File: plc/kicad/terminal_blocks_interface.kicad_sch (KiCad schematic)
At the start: 75 parts, among them CN1 DB128V-5.08-6P-GN-S, CN10 DB128V-5.08-2P-GN-S, CN4 KF128-5.0-3P, CN5 KF128-5.0-3P, CN7 DB128V-5.08-2P-GN-S, CN8 DB128V-5.08-2P-GN-S, CN9 DB128V-5.08-2P-GN-S, Q1 AO3400A, Q2 AO3400A, U1 LTV-814S-TA1-A, U10 LTV-814S-TA1-A, U4 ADS1115IDGSR, U5 TPS272C45DRHFR, U6 TPS272C45DRHFR, U7 TCA9535PWR, U8 LTV-814S-TA1-A, U9 LTV-814S-TA1-A

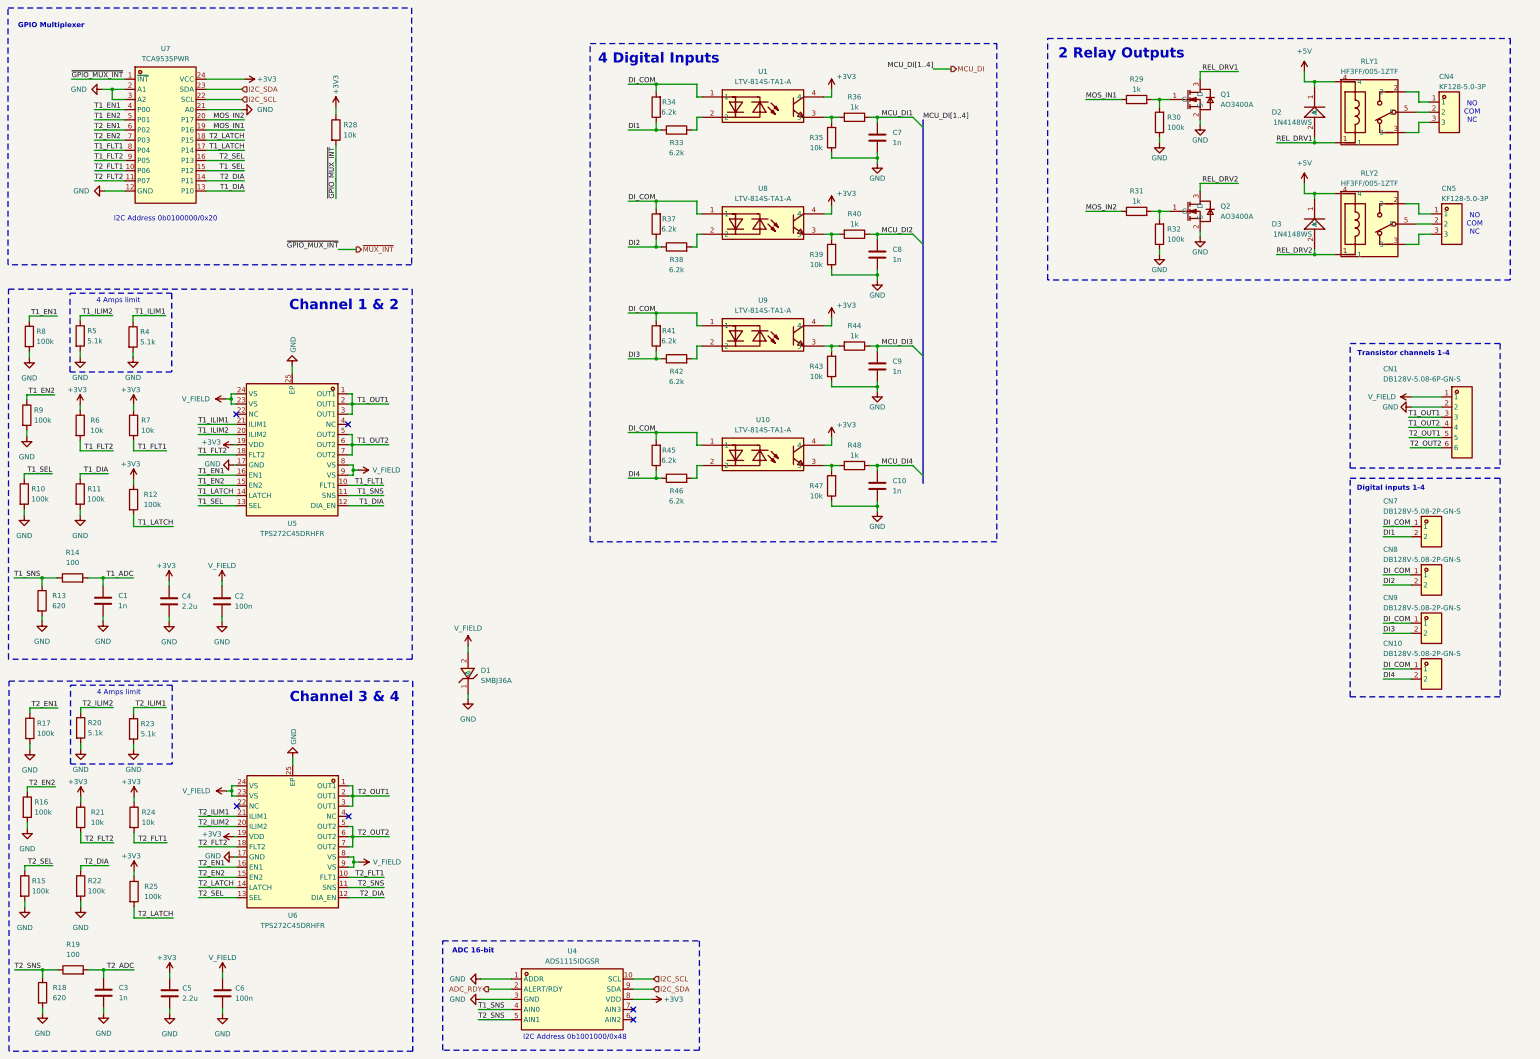
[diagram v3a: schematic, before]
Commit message: Added netclasses
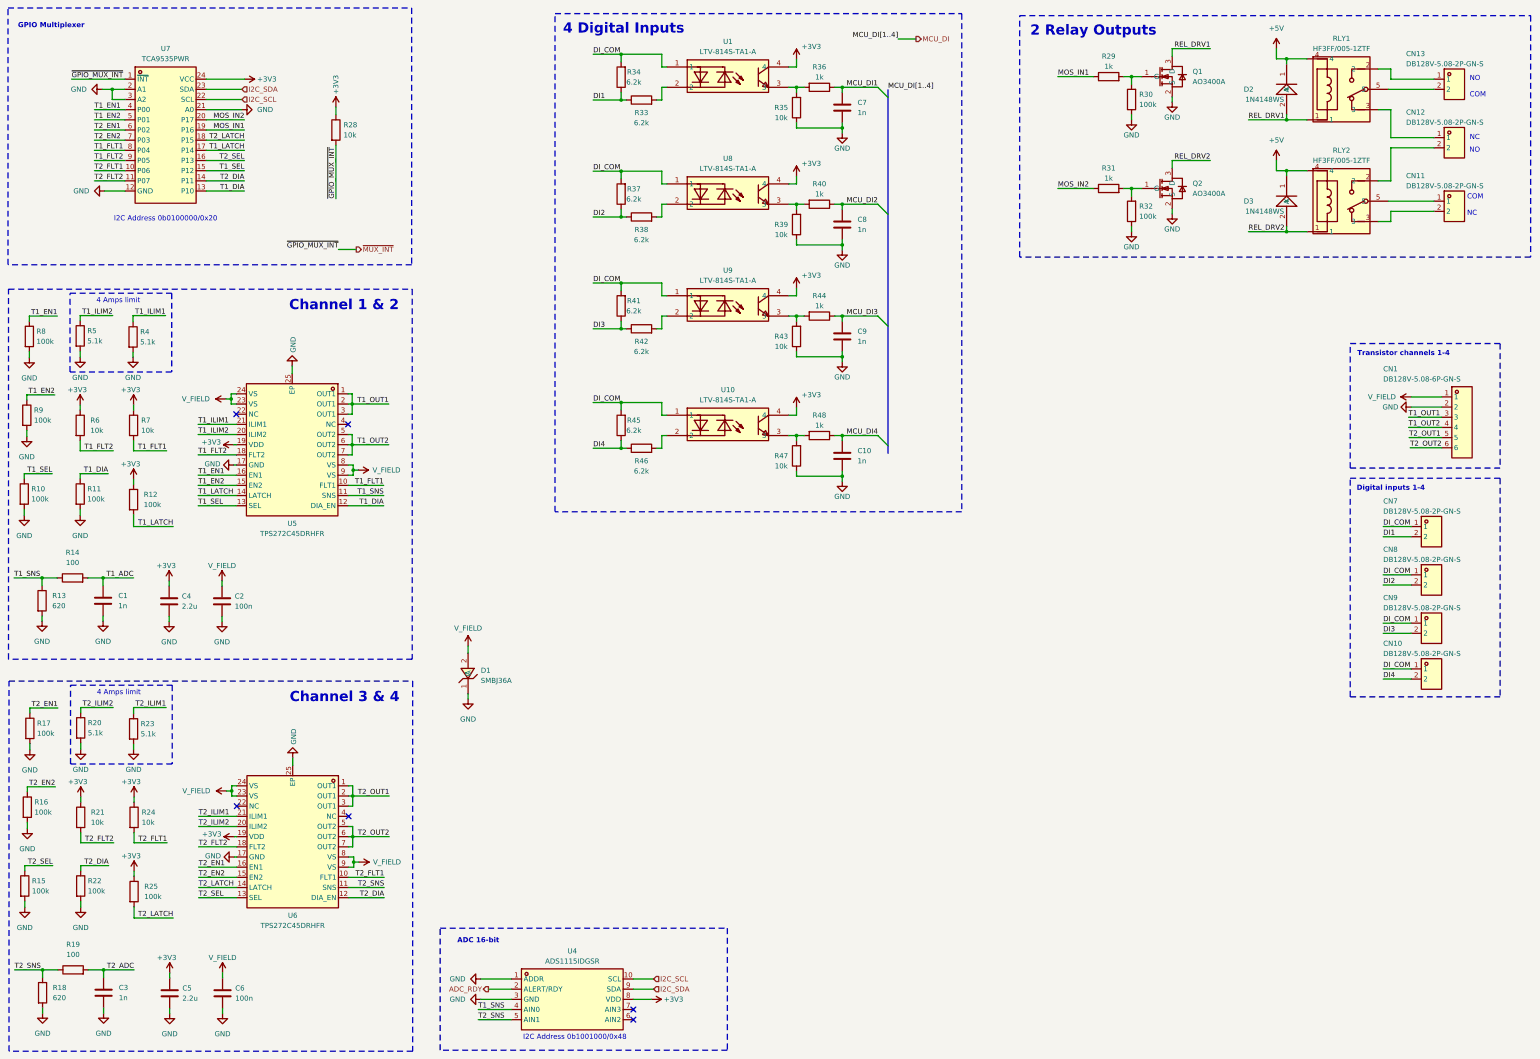
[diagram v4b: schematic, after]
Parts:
- removed CN4, CN5: KF128-5.0-3P, LibrePLC32:CONN-TH_3P-P5.00_KF128-5.0-3P, symbol LibrePLC32:KF128-5.0-3P
- added CN11, CN12, CN13: DB128V-5.08-2P-GN-S, LibrePLC32:CONN-TH_2P-P5.08_DIBO_DB128V-5.08, symbol LibrePLC32:DB128V-5.08-2P-GN-S
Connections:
- net at RLY1.2: now also CN13.1
- net at RLY1.3: now also CN12.1
- net at RLY1.5: now also CN13.2
- net at RLY2.2: now also CN12.2
- net at RLY2.3: now also CN11.2
- net at RLY2.5: now also CN11.1
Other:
- note added: "COM NC"
- note added: "NC"
- note added: "NO"
- note added: "NO COM"
- note removed: "NO COM NC"
- moved on the sheet: C10, C7, C8, C9, D2, D3, Q1, Q2, R29, R30, R31, R32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

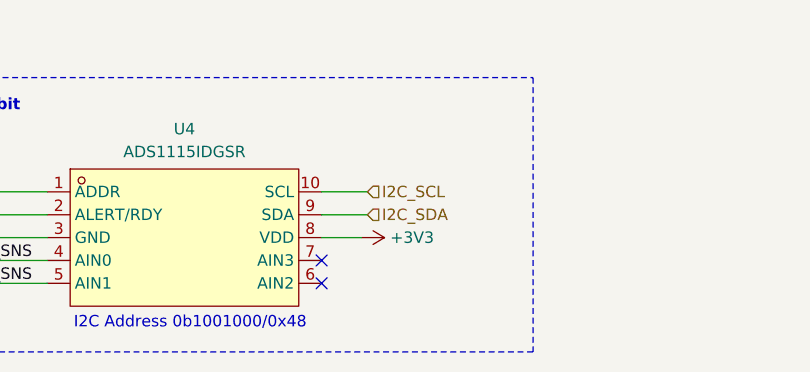
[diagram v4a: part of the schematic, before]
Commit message: Added the power protection IC
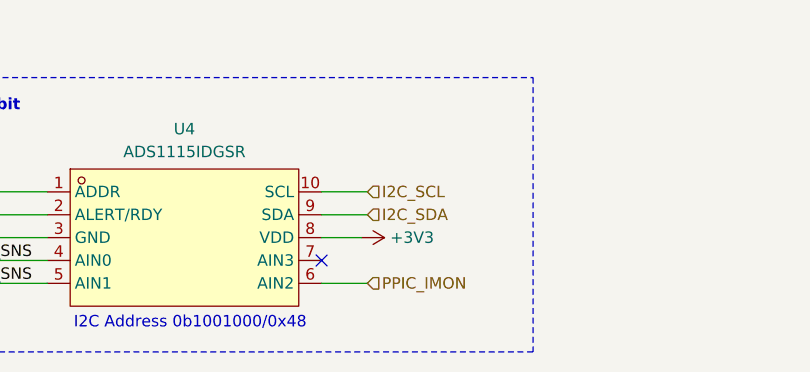
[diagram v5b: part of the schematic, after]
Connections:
- net PPIC_IMON: now reaches U4.6 (AIN2)
- no-connect marks 6 -> 5
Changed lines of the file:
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@@
 		(at 104.013 121.158)
 	)
-	(no_connect
-		(at 175.26 269.875)
-	)
 	(bus_entry
 		(at 236.347 66.167)
@@
 	(wire
 		(pts
+			(xy 175.26 269.875) (xy 180.34 269.875)
+		)
+		(stroke
+			(width 0)
+			(type default)
+		)
+	)
+	(wire
+		(pts
 			(xy 68.58 57.785) (xy 78.105 57.785)
 		)
@@
 		(effects
 			(font
+				(size 1.27 1.27)
+			)
+			(justify left)
+		)
+	)
+	(hierarchical_label "PPIC_IMON"
+		(shape input)
+		(at 180.34 269.875 0)
+		(effects
+			(font

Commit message: Wired ESP32-S3 preliminarily
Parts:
- added CN14: DB128V-5.08-2P-GN-S, LibrePLC32:CONN-TH_2P-P5.08_DIBO_DB128V-5.08, symbol LibrePLC32:DB128V-5.08-2P-GN-S
- added F1: BSMD1206C-1600T, LibrePLC32:F1206, symbol LibrePLC32:BSMD1206C-1600T
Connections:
- net GND: now also CN14.2
- new net: CN14.1, F1.2
- new net V_IN_MAIN: F1.1
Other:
- moved on the sheet: D1

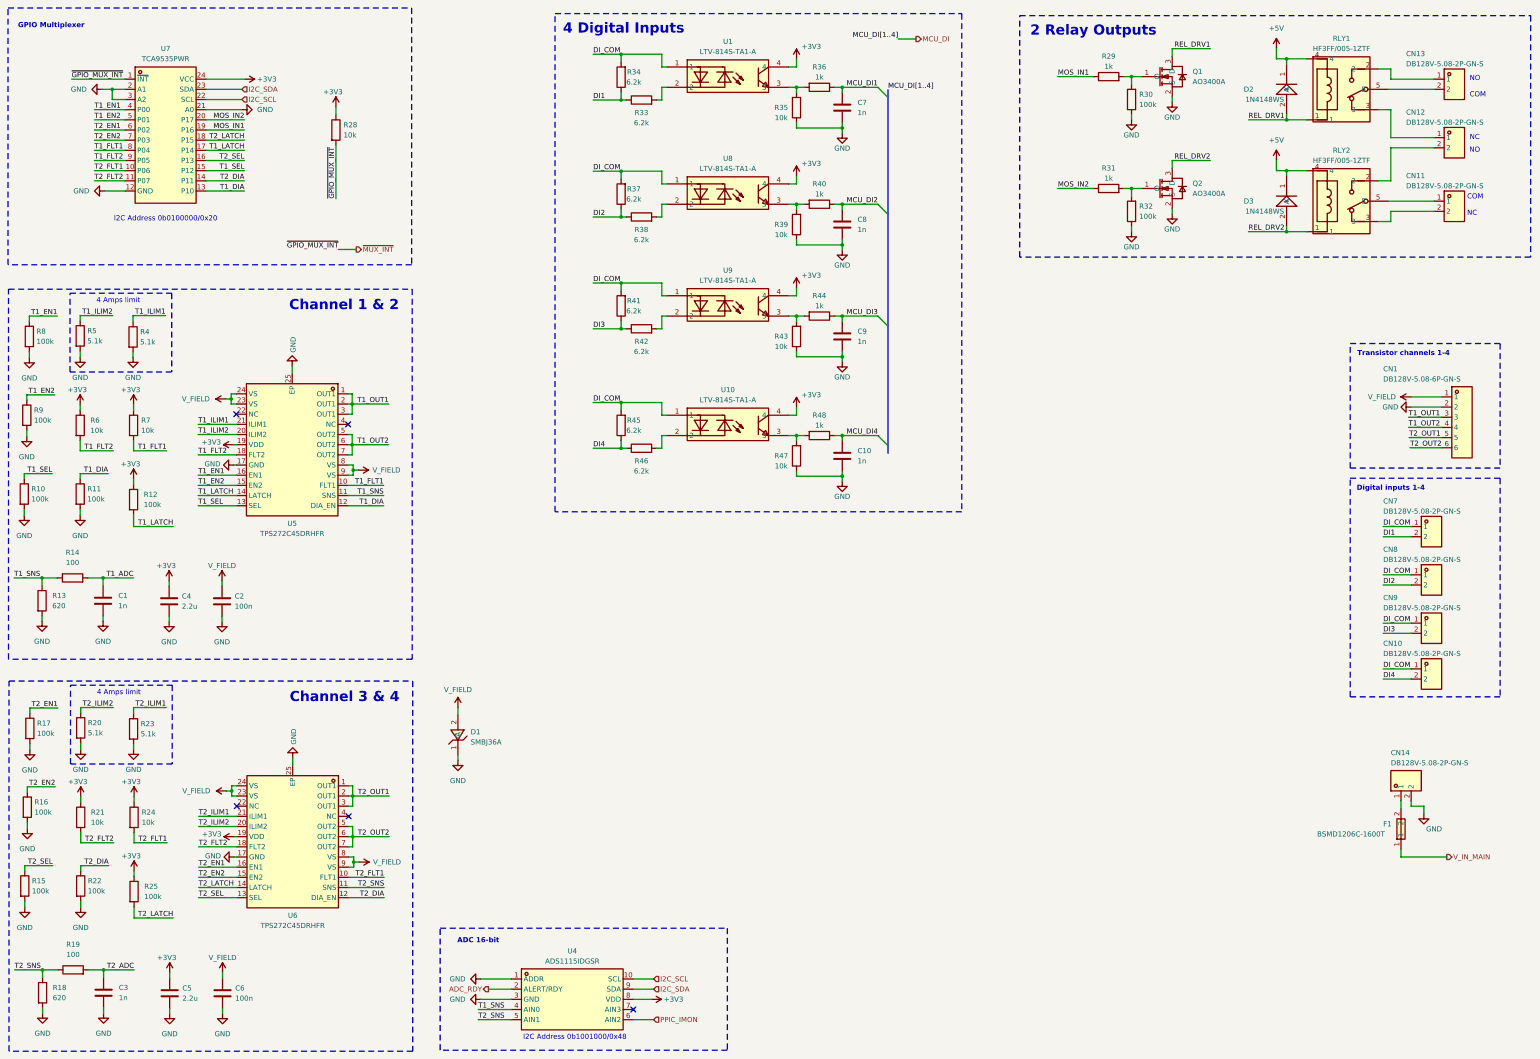
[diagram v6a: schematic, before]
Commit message: Added CP2102N bridge
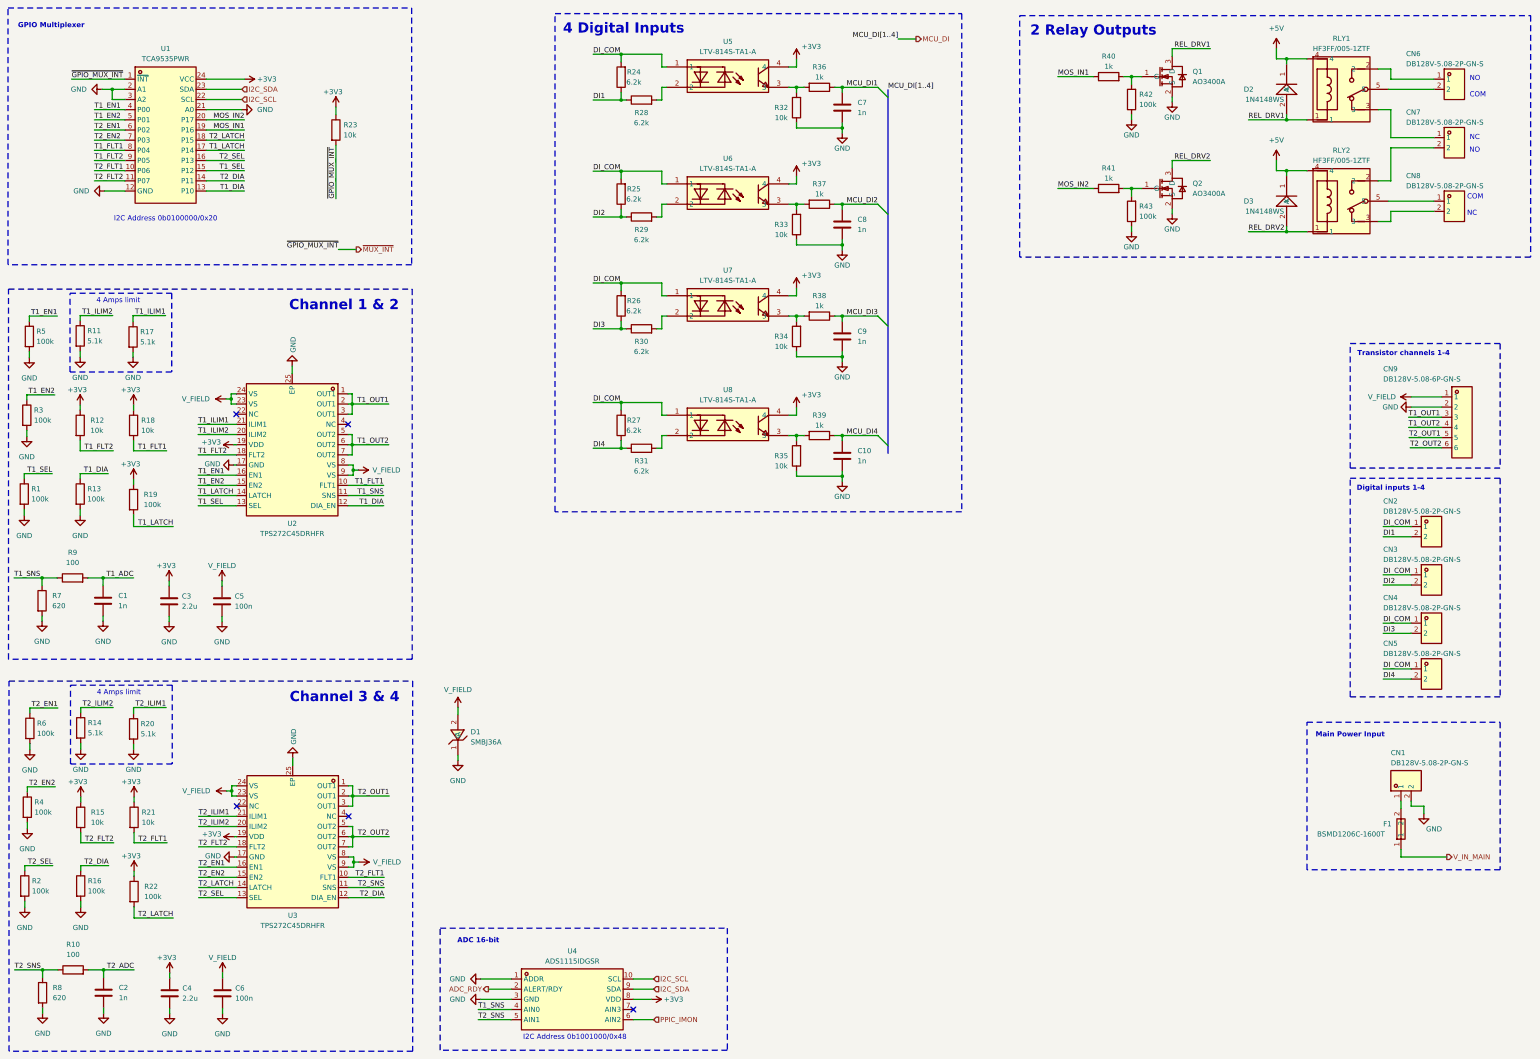
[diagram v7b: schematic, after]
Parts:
- renumbered C3 to C2, C4 to C3, C5 to C4, C2 to C5, CN14 to CN1, CN7 to CN2, CN8 to CN3, CN9 to CN4, CN10 to CN5, CN13 to CN6, CN12 to CN7, CN11 to CN8, CN1 to CN9, R10 to R1, R19 to R10, R5 to R11, R6 to R12, R11 to R13, R20 to R14, R21 to R15, R22 to R16, R4 to R17, R7 to R18, R12 to R19, R15 to R2, R23 to R20, R24 to R21, R25 to R22, R28 to R23, R34 to R24, R37 to R25, R41 to R26, R45 to R27, R33 to R28, R38 to R29, R9 to R3, R42 to R30, R46 to R31, R35 to R32, R39 to R33, R43 to R34, R47 to R35, R40 to R37, R44 to R38, R48 to R39, R16 to R4, R29 to R40, R31 to R41, R30 to R42, R32 to R43, R8 to R5, R17 to R6, R13 to R7, R18 to R8, R14 to R9, U7 to U1, U5 to U2, U6 to U3, U1 to U5, U8 to U6, U9 to U7, U10 to U8
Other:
- note added: "Main Power Input"

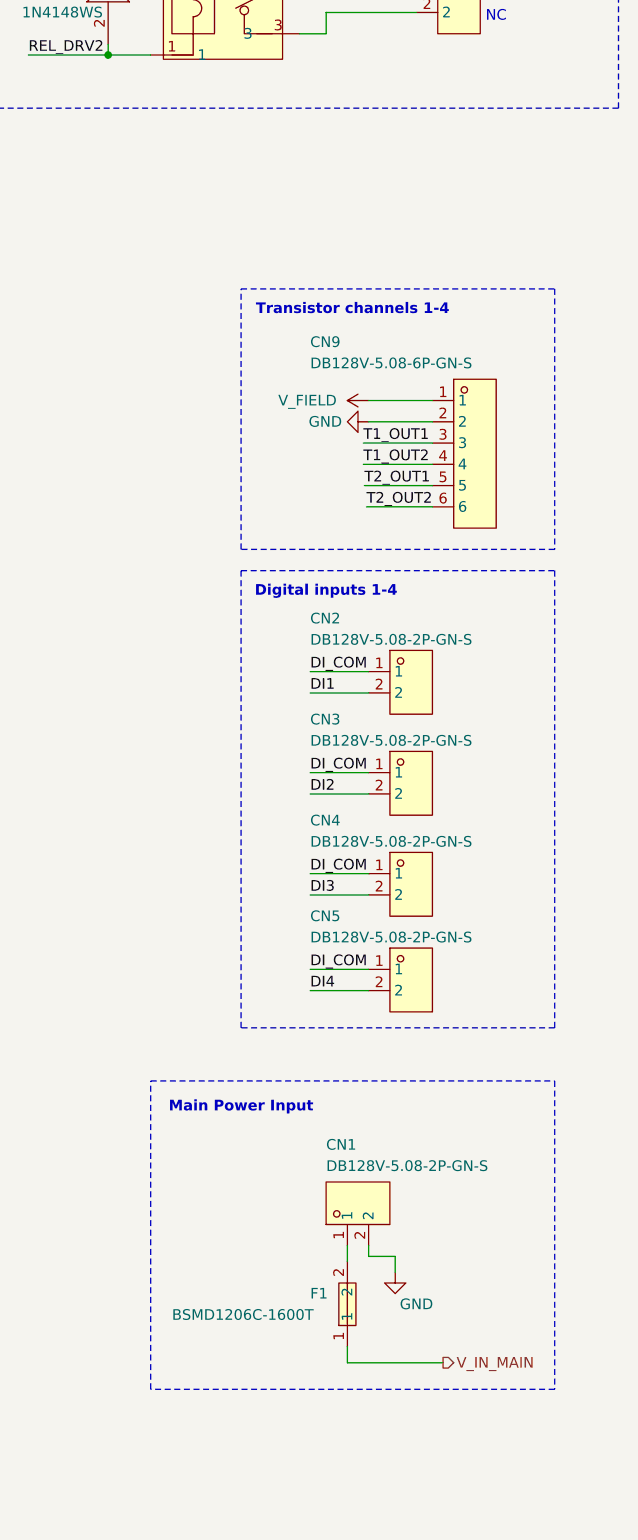
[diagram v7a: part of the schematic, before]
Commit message: Added 3.3V regulator
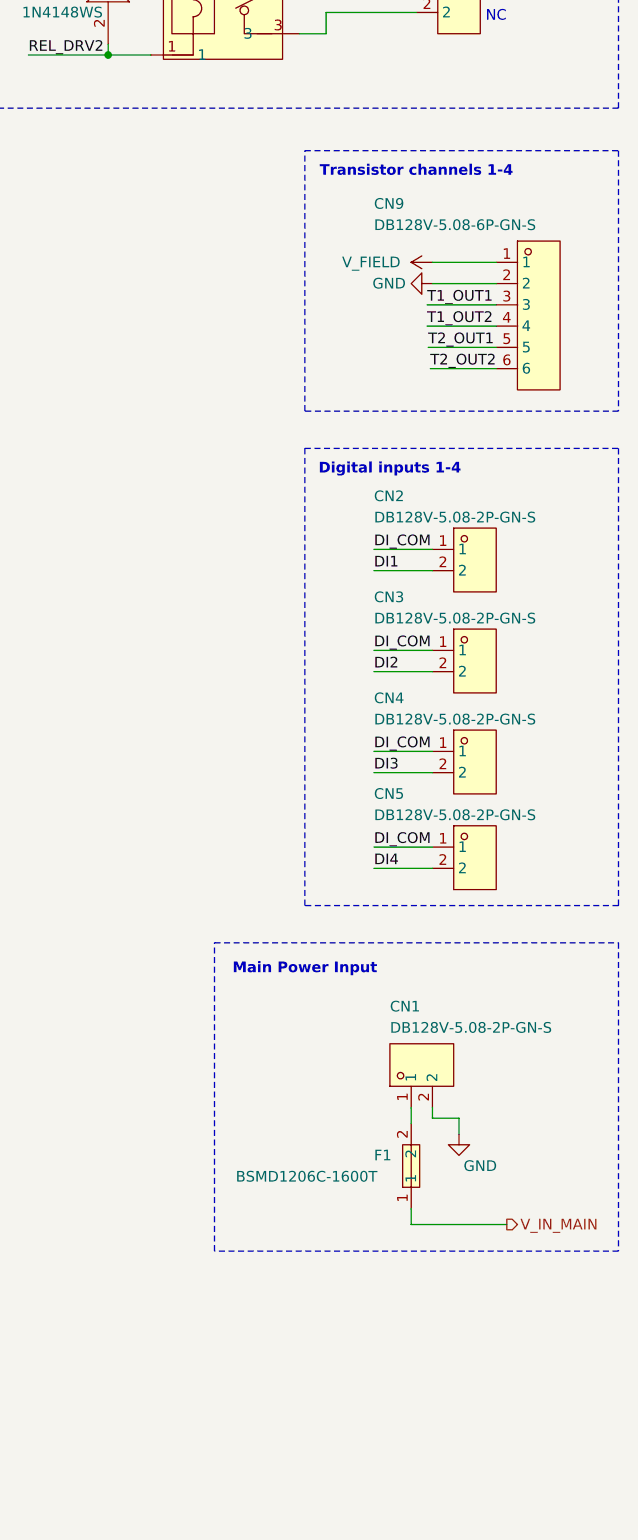
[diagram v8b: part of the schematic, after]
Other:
- moved on the sheet: CN1, CN2, CN3, CN4, CN5, CN9, F1
